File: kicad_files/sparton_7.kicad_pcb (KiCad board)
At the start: 6 copper layers, 100 x 50 mm, 143 parts, among them IC1 XC7S25-1CSGA225C, IC2 LTC3569EUDC#PBF, IC3 MBT3904DW1T1G, IC4 74AHCT125BQ-Q100,1, IC5 M74VHC1GT04DTT1G, J1 U254-051N-4BH806, Q1 SI2302CDS-T1-E3, Q2 MMBT4403LT3G, U1 MX25L3233FM2I-08G, U2 FT2232HQ, Y1 ABM3B-12.000MHZ-12-N2Y-T

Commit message: BGA Routing started
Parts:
- added C74: 100nf, Capacitor_SMD:C_0402_1005Metric_Pad0.74x0.62mm_HandSolder, F.Cu at (137.7, 61.3)
- added D12: LED_2, LED_SMD:LED_0603_1608Metric_Pad1.05x0.95mm_HandSolder, F.Cu at (149.6, 89.9)
- added D13: LED_3, LED_SMD:LED_0603_1608Metric_Pad1.05x0.95mm_HandSolder, F.Cu at (148.0, 89.9)
- added D14: LED_4, LED_SMD:LED_0603_1608Metric_Pad1.05x0.95mm_HandSolder, F.Cu at (146.3, 89.9)
- added D9: LED_1, LED_SMD:LED_0603_1608Metric_Pad1.05x0.95mm_HandSolder, F.Cu at (151.2, 89.9)
- added FB1: L_Ferrite, LED_SMD:LED_0603_1608Metric_Pad1.05x0.95mm_HandSolder, B.Cu at (144.1, 75.8)
- added IC6: M93C46-WMN6TP, SamacSys_Parts:SOIC127P600X175-8N, F.Cu at (137.0, 64.8)
- added L4: 1K 100MHz, Inductor_SMD:L_0402_1005Metric_Pad0.77x0.64mm_HandSolder, B.Cu at (128.4, 74.7)
- added L5: 1K 100MHz, Inductor_SMD:L_0402_1005Metric_Pad0.77x0.64mm_HandSolder, B.Cu at (128.4, 77.2)
- added R58: 0, Resistor_SMD:R_0402_1005Metric_Pad0.72x0.64mm_HandSolder, F.Cu at (136.4, 76.4)
- added R59: 0, Resistor_SMD:R_0402_1005Metric_Pad0.72x0.64mm_HandSolder, F.Cu at (136.4, 79.5)
- added R60: 0, Resistor_SMD:R_0402_1005Metric_Pad0.72x0.64mm_HandSolder, F.Cu at (136.4, 80.6)
- added R61: 0, Resistor_SMD:R_0402_1005Metric_Pad0.72x0.64mm_HandSolder, F.Cu at (136.4, 75.3)
- added R62: 0, Resistor_SMD:R_0402_1005Metric_Pad0.72x0.64mm_HandSolder, F.Cu at (141.4, 63.5)
- added R63: 0, Resistor_SMD:R_0402_1005Metric_Pad0.72x0.64mm_HandSolder, F.Cu at (141.4, 66.0)
- added R64: 2.2K, Resistor_SMD:R_0402_1005Metric_Pad0.72x0.64mm_HandSolder, F.Cu at (132.1, 66.7)
- added R65: 10K, Resistor_SMD:R_0402_1005Metric_Pad0.72x0.64mm_HandSolder, F.Cu at (137.7, 59.2)
- added R66: 10K, Resistor_SMD:R_0402_1005Metric_Pad0.72x0.64mm_HandSolder, F.Cu at (137.7, 60.3)
- added R67: 10K, Resistor_SMD:R_0402_1005Metric_Pad0.72x0.64mm_HandSolder, F.Cu at (132.1, 67.8)
- added R68: 330, Resistor_SMD:R_0402_1005Metric_Pad0.72x0.64mm_HandSolder, F.Cu at (151.2, 87.0)
- added R69: 330, Resistor_SMD:R_0402_1005Metric_Pad0.72x0.64mm_HandSolder, F.Cu at (149.6, 87.1)
- added R70: 330, Resistor_SMD:R_0402_1005Metric_Pad0.72x0.64mm_HandSolder, F.Cu at (148.0, 87.1)
- added R71: 330, Resistor_SMD:R_0402_1005Metric_Pad0.72x0.64mm_HandSolder, F.Cu at (146.3, 87.1)
- C10, C11, C12, C13, C14, C15, C16, C19, C8, C9: moved to B.Cu
- IC4: footprint SamacSys_Parts:74AHCT125BQQ1001 -> SamacSys_Parts:SOIC127P600X175-14N
- moved R31 85.5 mm to (105.3, 54.3)
- moved R32 80.4 mm to (111.4, 53.0), turned to 180 degrees
- moved R36 78.5 mm to (113.8, 67.1), turned to 90 degrees
- moved R37 77.9 mm to (114.3, 68.8), turned to 180 degrees
- moved C45 74.1 mm to (108.6, 58.2), turned to 180 degrees
- moved R24 72.6 mm to (113.5, 62.9), turned to -90 degrees
- moved D4 71.6 mm to (114.9, 67.1), turned to -90 degrees
- moved R23 71.4 mm to (114.5, 62.9), turned to 90 degrees
- moved IC3 50.3 mm to (108.4, 53.7), turned to 180 degrees
- moved R39 40.1 mm to (124.0, 69.1), turned to -90 degrees
- moved Q2 40.0 mm to (128.3, 55.8)
- moved R40 38.8 mm to (126.1, 69.1), turned to -90 degrees
- moved R38 38.3 mm to (125.0, 69.1), turned to -90 degrees
- moved R9 37.9 mm to (147.4, 68.4), turned to 90 degrees
- moved R10 37.6 mm to (148.6, 68.4), turned to 90 degrees
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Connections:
- net /FTDI/USB_DM renamed /FTDI/USB_D-
- net /FTDI/USB_DP renamed /FTDI/USB_D+
- C44 pad 2: /FPGA_SPARTAN_7/CONFIG/GND -> GND
- D1 pad 1: /FPGA_SPARTAN_7/CONFIG/GND -> GND
- IC1 pad J8: /FPGA_SPARTAN_7/CONFIG/GND -> GND
- IC1 pad J9: /FPGA_SPARTAN_7/CONFIG/GND -> GND
- IC1 pad K1: /FPGA_SPARTAN_7/BANK_34/LED1 -> /FPGA_SPARTAN_7/BANK_34/LED2
- IC1 pad K15: /FPGA_SPARTAN_7/BANK_14/UART_RXD_OUT -> /FPGA_SPARTAN_7/BANK_14/UART_TXD_IN
- R4 pad 2: /FPGA_SPARTAN_7/CONFIG/GND -> GND
- R48 pad 2: /FTDI/TXD -> /FPGA_SPARTAN_7/TXD
- R49 pad 2: /FTDI/RXD -> /FPGA_SPARTAN_7/RXD
- R5 pad 2: /FPGA_SPARTAN_7/CONFIG/GND -> GND
- U1 pad 4: /FPGA_SPARTAN_7/CONFIG/GND -> GND
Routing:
- net GND: track 0.00 -> 88.1 mm, vias 0 -> 36
- net +3V3: track 0.00 -> 67.2 mm, vias 0 -> 8
- net /FPGA_SPARTAN_7/TDI_FPGA: track 0.00 -> 45.0 mm, vias 0 -> 2
- net /FPGA_SPARTAN_7/TDO_FPGA: track 0.00 -> 41.2 mm, vias 0 -> 2
- net /FPGA_SPARTAN_7/VCC1V0: track 0.00 -> 33.0 mm, vias 0 -> 11
- net /FPGA_SPARTAN_7/TCLK: track 0.00 -> 31.2 mm, vias 0 -> 2
- net /FPGA_SPARTAN_7/TMS: track 0.00 -> 30.1 mm, vias 0 -> 2
- net /FTDI/FT_TCK: track 0.00 -> 24.6 mm
- net /FTDI/EECS: track 0.00 -> 21.5 mm
- net /FTDI/EECLK: track 0.00 -> 19.6 mm
- net /FTDI/FT_TDI: track 0.00 -> 16.1 mm
- net /FTDI/ESP_EN_N: track 0.00 -> 15.2 mm
- net /FPGA_SPARTAN_7/VCC1V8: track 0.00 -> 14.7 mm, vias 0 -> 2
- net /FTDI/EEDATA: track 0.00 -> 12.7 mm
- net /FTDI/USB_D+: track 0.00 -> 12.2 mm, vias 0 -> 1
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- added copper zone on In3.Cu, net /FPGA_SPARTAN_7/VCC1V0
- added copper zone on F.Cu, net GND
- added copper zone on In1.Cu, net GND

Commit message: pcb layout updated
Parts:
- added C1: 10nf, Capacitor_SMD:C_0402_1005Metric_Pad0.74x0.62mm_HandSolder, B.Cu at (145.9, 74.8)
- added C2: 470nf, Capacitor_SMD:C_0402_1005Metric_Pad0.74x0.62mm_HandSolder, B.Cu at (146.5, 73.2)
- added C3: 470nf, Capacitor_SMD:C_0402_1005Metric_Pad0.74x0.62mm_HandSolder, B.Cu at (143.1, 78.6)
- added C4: 4.7uf, Capacitor_SMD:C_0603_1608Metric, F.Cu at (85.8, 60.0)
- added C5: 100uf, Capacitor_SMD:C_1210_3225Metric, F.Cu at (93.3, 64.5)
- added C6: 470nf, Capacitor_SMD:C_0402_1005Metric_Pad0.74x0.62mm_HandSolder, F.Cu at (96.9, 58.1)
- added C72: 1uf, Capacitor_SMD:C_0402_1005Metric_Pad0.74x0.62mm_HandSolder, F.Cu at (143.2, 67.2)
- added C73: 1uf, Capacitor_SMD:C_0402_1005Metric_Pad0.74x0.62mm_HandSolder, F.Cu at (145.7, 67.2)
- added FB2: L_Ferrite, Inductor_SMD:L_0603_1608Metric_Pad1.05x0.95mm_HandSolder, B.Cu at (148.1, 72.8)
- added J2: Conn_02x10_Odd_Even, Connector_PinHeader_1.27mm:PinHeader_2x10_P1.27mm_Vertical_SMD, F.Cu at (164.9, 55.5)
- added J3: Conn_02x05_Odd_Even, Connector_PinHeader_1.27mm:PinHeader_2x05_P1.27mm_Vertical_SMD, F.Cu at (145.1, 55.5)
- added J4: Conn_02x06_Odd_Even, Connector_PinHeader_1.27mm:PinHeader_2x06_P1.27mm_Vertical_SMD, F.Cu at (153.5, 55.5)
- added L1: 1.5uH, Inductor_SMD:L_0805_2012Metric, F.Cu at (92.3, 55.6)
- added L2: 3.3uH, Inductor_SMD:L_0805_2012Metric, F.Cu at (92.3, 58.3)
- added L3: 2.2uH, Inductor_SMD:L_0805_2012Metric, F.Cu at (92.3, 61.1)
- C17, C18, C30, C31, C32, C7, R1, R2: moved to B.Cu
- FB1: footprint LED_SMD:LED_0603_1608Metric_Pad1.05x0.95mm_HandSolder -> Inductor_SMD:L_0603_1608Metric_Pad1.05x0.95mm_HandSolder
- moved C67 60.8 mm to (110.0, 81.2)
- moved R45 50.0 mm to (113.4, 81.2)
- moved R14 46.5 mm to (148.5, 60.5)
- moved C64 44.5 mm to (127.3, 71.0), turned to 180 degrees
- moved R16 42.1 mm to (151.1, 60.5), turned to 180 degrees
- moved C44 41.0 mm to (155.7, 60.3), turned to 180 degrees
- moved C61 39.2 mm to (128.4, 83.2), turned to -90 degrees
- moved C62 37.2 mm to (130.5, 83.2), turned to -90 degrees
- moved C56 37.0 mm to (132.1, 69.7)
- moved C63 36.1 mm to (133.6, 75.7), turned to 90 degrees
- moved R12 34.2 mm to (154.3, 69.0)
- moved R2 33.0 mm to (145.0, 72.9), turned to 90 degrees
- moved R1 32.8 mm to (148.3, 79.5), turned to 90 degrees
- moved R56 31.9 mm to (142.6, 63.1), turned to -90 degrees
- moved R57 31.4 mm to (145.1, 63.1), turned to -90 degrees
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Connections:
- R3 pad 1: /FPGA_SPARTAN_7/CONFIG/VCC_3V3 -> +3V3
- R6 pad 1: /FPGA_SPARTAN_7/CONFIG/VCC_3V3 -> +3V3
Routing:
- net +3V3: track 67.2 -> 96.6 mm, vias 8 -> 12
- net /FPGA_SPARTAN_7/CONFIG/QSPI_SCK: track 9.96 -> 29.7 mm, vias 1 -> 2
- net /FTDI/ESP_EN_N: track 15.2 -> 34.8 mm, vias 0 -> 2
- net /FPGA_SPARTAN_7/BANK_14/UART_TXD_IN: track 3.71 -> 21.8 mm, vias 1 -> 2
- net /FPGA_SPARTAN_7/BANK_14/UART_RXD_OUT: track 7.38 -> 23.3 mm, vias 1 -> 2
- net /FPGA_SPARTAN_7/BANK_15/AIN33_P: track 0.57 -> 13.5 mm
- net /FPGA_SPARTAN_7/BANK_15/AIN32_P: track 0.57 -> 13.0 mm
- net /FPGA_SPARTAN_7/BANK_15/AIN33_N: track 0.57 -> 12.7 mm
- net /FPGA_SPARTAN_7/BANK_15/AIN32_N: track 0.57 -> 12.3 mm
- net Net-(IC1A-VCCO_15_1): track 1.13 -> 12.7 mm, vias 2 -> 3
- net /FPGA_SPARTAN_7/CONFIG/QSPI_DQ0: track 0.57 -> 10.0 mm, vias 1 -> 2
- net /FPGA_SPARTAN_7/CONFIG/MODE_2: track 0.57 -> 9.78 mm, vias 1 -> 2
- net Net-(D7-A): track 0.00 -> 7.58 mm
- net /FPGA_SPARTAN_7/CONFIG/MODE_1: track 0.57 -> 7.73 mm, vias 1 -> 2
- net Net-(U1-WP#/SIO2): track 6.00 -> 12.6 mm
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
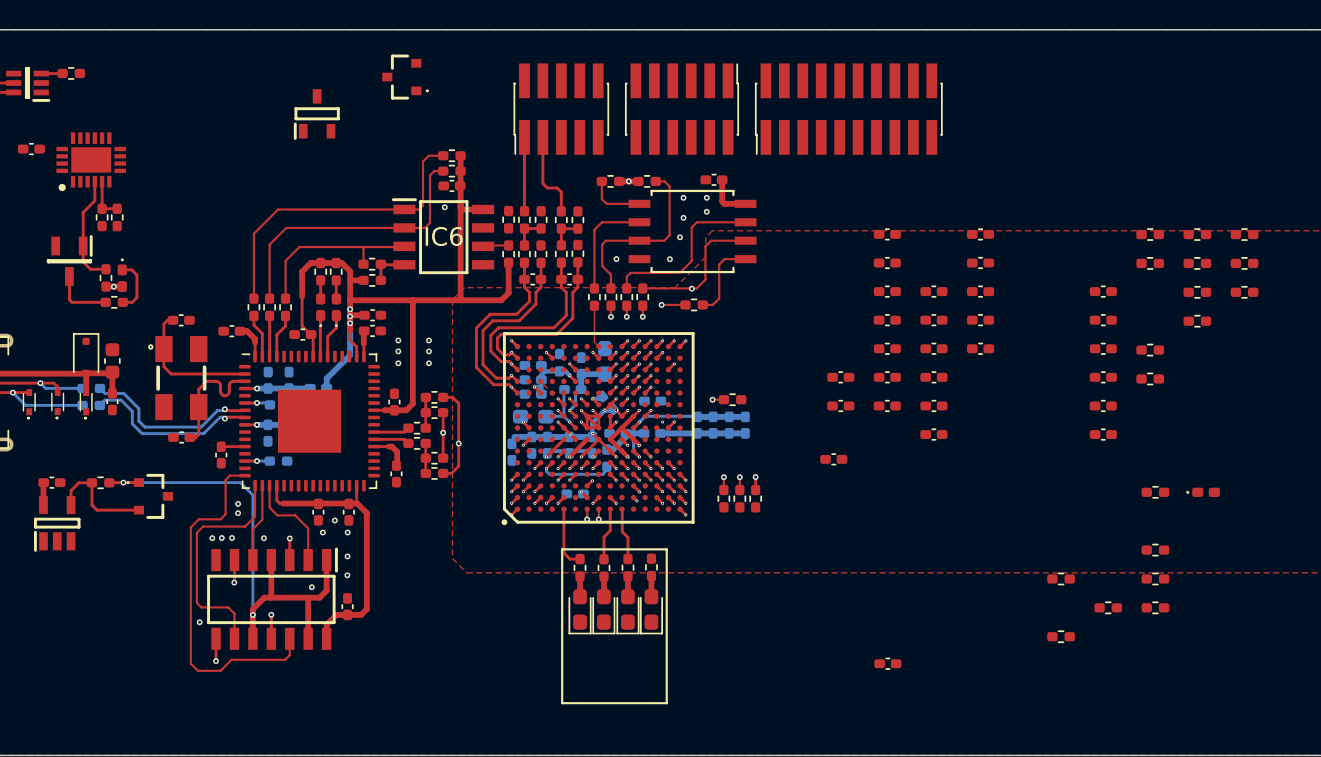
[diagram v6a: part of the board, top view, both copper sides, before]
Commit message: updated layout
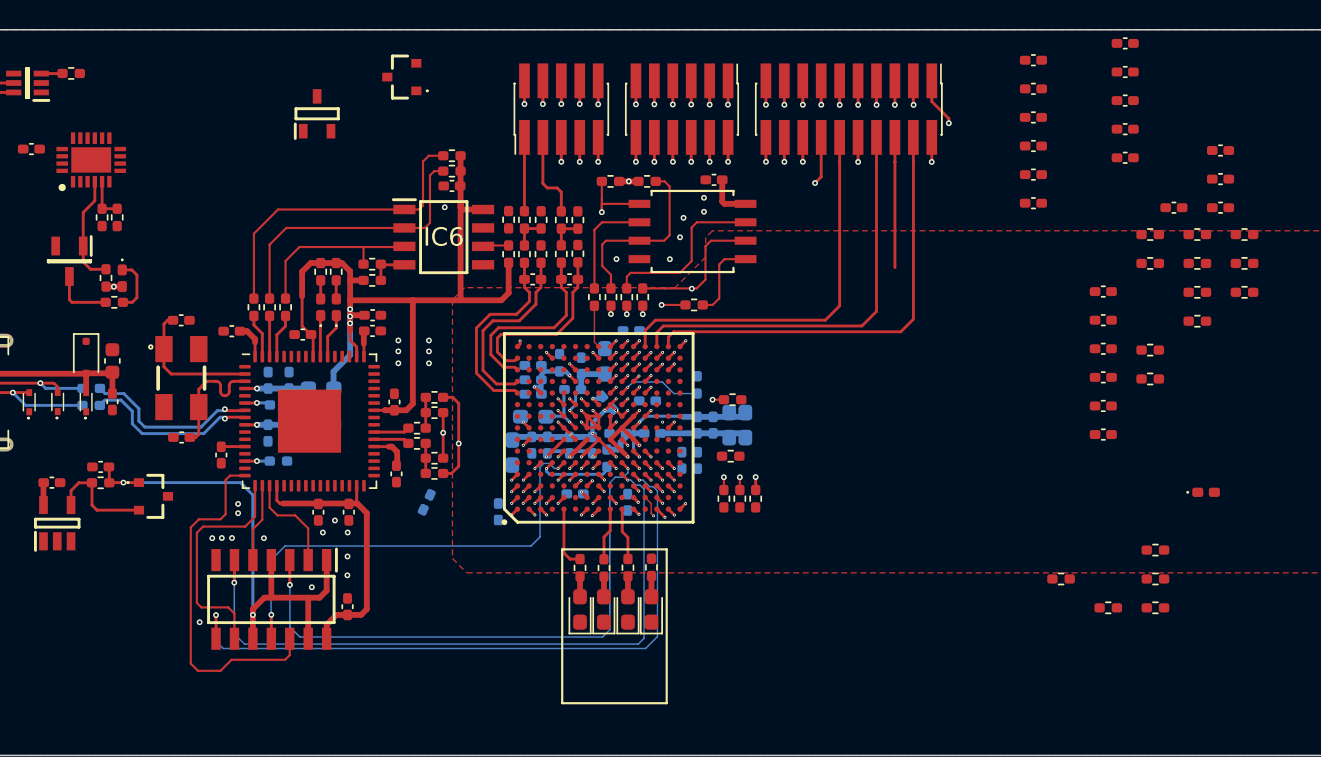
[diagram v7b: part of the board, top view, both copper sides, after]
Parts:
- C10, C11, C18: footprint Capacitor_SMD:C_0402_1005Metric_Pad0.74x0.62mm_HandSolder -> Capacitor_SMD:C_0603_1608Metric_Pad1.08x0.95mm_HandSolder
- C20, C22, C23, C24, C25, C26, R8: moved to B.Cu
- L4, L5: footprint Inductor_SMD:L_0402_1005Metric_Pad0.77x0.64mm_HandSolder -> Inductor_SMD:L_0603_1608Metric_Pad1.05x0.95mm_HandSolder
- moved C66 55.9 mm to (113.4, 80.1), turned to 180 degrees
- moved C25 34.9 mm to (135.9, 82.6), turned to -115 degrees
- moved R8 30.5 mm to (154.5, 74.5), turned to -90 degrees
- moved C26 29.9 mm to (140.8, 83.2), turned to -90 degrees
- moved R15 29.4 mm to (156.8, 79.4)
- moved C27 26.7 mm to (190.6, 58.3)
- moved C28 26.7 mm to (190.6, 60.3)
- moved C29 26.7 mm to (190.6, 62.3)
- moved C21 26.7 mm to (187.3, 62.3)
- moved C23 21.0 mm to (153.4, 79.7), turned to 90 degrees
- moved C24 18.9 mm to (154.5, 79.7), turned to 90 degrees
- moved C33 17.4 mm to (177.7, 52.1)
- moved C34 17.4 mm to (177.7, 54.1)
- moved C35 17.4 mm to (177.7, 56.0)
- moved C36 17.4 mm to (177.7, 58.0)
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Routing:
- net /FPGA_SPARTAN_7/BANK_34/PIO09: track 0.00 -> 76.0 mm, vias 0 -> 2
- net /FPGA_SPARTAN_7/BANK_34/JA7: track 0.00 -> 67.7 mm, vias 0 -> 2
- net /FPGA_SPARTAN_7/BANK_34/PIO42: track 0.00 -> 63.8 mm, vias 0 -> 2
- net /FPGA_SPARTAN_7/BANK_34/JA4: track 0.00 -> 59.9 mm, vias 0 -> 2
- net /FPGA_SPARTAN_7/BANK_34/PIO43: track 0.00 -> 56.9 mm, vias 0 -> 2
- net /FPGA_SPARTAN_7/BANK_34/PIO44: track 0.00 -> 55.7 mm, vias 0 -> 2
- net /FPGA_SPARTAN_7/BANK_34/PIO01: track 0.00 -> 54.7 mm, vias 0 -> 2
- net /FPGA_SPARTAN_7/BANK_34/PIO02: track 0.57 -> 54.4 mm, vias 1 -> 2
- net /FPGA_SPARTAN_7/BANK_34/JA3: track 0.00 -> 53.3 mm, vias 0 -> 2
- net /FPGA_SPARTAN_7/BANK_34/PIO08: track 0.00 -> 52.1 mm, vias 0 -> 2
- net /FPGA_SPARTAN_7/BANK_34/PIO03: track 0.00 -> 51.4 mm, vias 0 -> 2
- net /FPGA_SPARTAN_7/BANK_14/PIO16: track 0.00 -> 46.7 mm, vias 0 -> 2
- net /FPGA_SPARTAN_7/BANK_34/PIO05: track 0.00 -> 46.6 mm, vias 0 -> 2
- net /FPGA_SPARTAN_7/BANK_34/PIO04: track 0.57 -> 46.4 mm, vias 1 -> 2
- net /FPGA_SPARTAN_7/BANK_34/JA1: track 0.57 -> 44.8 mm, vias 1 -> 2
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
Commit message: layout basic completed
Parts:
- added kibuzzard-6474970A: G***, kibuzzard-6474970A, F.Cu at (151.3, 93.3)
- added kibuzzard-64749717: G***, kibuzzard-64749717, F.Cu at (149.8, 93.4)
- added kibuzzard-64749722: G***, kibuzzard-64749722, F.Cu at (148.1, 93.4)
- added kibuzzard-6474973D: G***, kibuzzard-6474973D, F.Cu at (146.5, 93.4)
- C21, C33, C34, C35, C36, C37, C38, C6: moved to B.Cu
- C27, C28, C42, C43: footprint Capacitor_SMD:C_0402_1005Metric_Pad0.74x0.62mm_HandSolder -> Capacitor_SMD:C_0603_1608Metric_Pad1.08x0.95mm_HandSolder; moved to B.Cu
- C29: footprint Capacitor_SMD:C_0402_1005Metric_Pad0.74x0.62mm_HandSolder -> Capacitor_SMD:C_1206_3216Metric_Pad1.33x1.80mm_HandSolder; moved to B.Cu
- C4: footprint Capacitor_SMD:C_0603_1608Metric -> Capacitor_SMD:C_0603_1608Metric_Pad1.08x0.95mm_HandSolder; moved to B.Cu
- C45, C48: footprint Capacitor_SMD:C_0402_1005Metric_Pad0.74x0.62mm_HandSolder -> Capacitor_SMD:C_0805_2012Metric_Pad1.18x1.45mm_HandSolder
- C5: footprint Capacitor_SMD:C_1210_3225Metric -> Capacitor_SMD:C_1206_3216Metric_Pad1.33x1.80mm_HandSolder; moved to B.Cu
- C50, C52, C7: footprint Capacitor_SMD:C_0402_1005Metric_Pad0.74x0.62mm_HandSolder -> Capacitor_SMD:C_0603_1608Metric_Pad1.08x0.95mm_HandSolder
- R8: moved to F.Cu
- moved R33 87.0 mm to (105.3, 63.9), turned to 90 degrees
- moved R29 78.4 mm to (111.6, 55.2), turned to -90 degrees
- moved R30 77.7 mm to (112.7, 55.2), turned to 90 degrees
- moved R22 75.5 mm to (110.6, 58.7), turned to 180 degrees
- moved R21 75.3 mm to (110.6, 59.7)
- moved C51 74.8 mm to (110.6, 55.2), turned to -90 degrees
- moved C52 74.3 mm to (109.2, 65.5), turned to 180 degrees
- moved R25 72.9 mm to (114.8, 55.2), turned to -90 degrees
- moved R27 72.5 mm to (117.0, 55.2), turned to -90 degrees
- moved R26 72.4 mm to (115.8, 55.2), turned to 90 degrees
- moved R28 70.8 mm to (119.0, 55.2), turned to 90 degrees
- moved C47 69.9 mm to (113.8, 55.2), turned to -90 degrees
- moved C49 66.6 mm to (118.0, 55.2), turned to -90 degrees
- moved R35 65.5 mm to (128.6, 52.5), turned to 90 degrees
- moved R34 64.4 mm to (128.2, 58.8), turned to 180 degrees
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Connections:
- R41 pad 1: /FTDI/VDD3V3 -> +3V3
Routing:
- net +3V3: track 95.7 -> 260.6 mm, vias 12 -> 35
- net /FPGA_SPARTAN_7/VCC1V0: track 39.5 -> 117.6 mm, vias 18 -> 23
- net /POWER_REGULATOR/VU: track 0.00 -> 44.1 mm, vias 0 -> 10
- net /FPGA_SPARTAN_7/BANK_14/PIO18: track 9.52 -> 31.7 mm, vias 1 -> 2
- net /FPGA_SPARTAN_7/VCC1V8: track 17.8 -> 36.6 mm
- net /FPGA_SPARTAN_7/CONFIG/DONE: track 0.57 -> 15.3 mm, vias 1 -> 2
- net /FPGA_SPARTAN_7/CONFIG/PROG: track 0.57 -> 13.6 mm, vias 1 -> 2
- net Net-(IC1E-CFGBVS_0): track 0.57 -> 13.5 mm, vias 1 -> 2
- net /FPGA_SPARTAN_7/BANK_34/LED1: track 0.57 -> 11.5 mm, vias 1 -> 2
- net /POWER_REGULATOR/EN2: track 1.47 -> 12.0 mm
- net Net-(IC1A-VCCO_15_1): track 12.7 -> 21.6 mm
- net /FPGA_SPARTAN_7/CONFIG/INIT: track 0.57 -> 8.08 mm, vias 1 -> 2
- net Net-(IC2-FB3): track 0.00 -> 7.16 mm
- net Net-(IC2-FB2): track 0.00 -> 7.12 mm
- net Net-(D3-K): track 0.00 -> 6.93 mm
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- added copper zone on F.Cu, net +3V3
- added copper zone on In4.Cu, net +3V3
- added copper zone on F.Cu, net /FPGA_SPARTAN_7/VCC1V0
- added copper zone on F.Cu, net /POWER_REGULATOR/VU
- added copper zone on In4.Cu, net GND
- added copper zone on F.Cu, net Net-(IC2-SW1)
- added copper zone on F.Cu, net Net-(IC2-SW2)
- added copper zone on F.Cu, net Net-(IC2-SW3)
- added copper zone on F.Cu, net Net-(IC3-B_1)
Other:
- board size 100 x 50 mm -> 75 x 50 mm
